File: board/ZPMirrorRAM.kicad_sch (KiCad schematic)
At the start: 15 parts, among them U10 74LS260, U11 74F86, U15 74F00, U21 CY7C192, U22 CY7C192, U23 74F11, U24 74LS154, U25 74F138, U34 74ACT14, U9 74F08

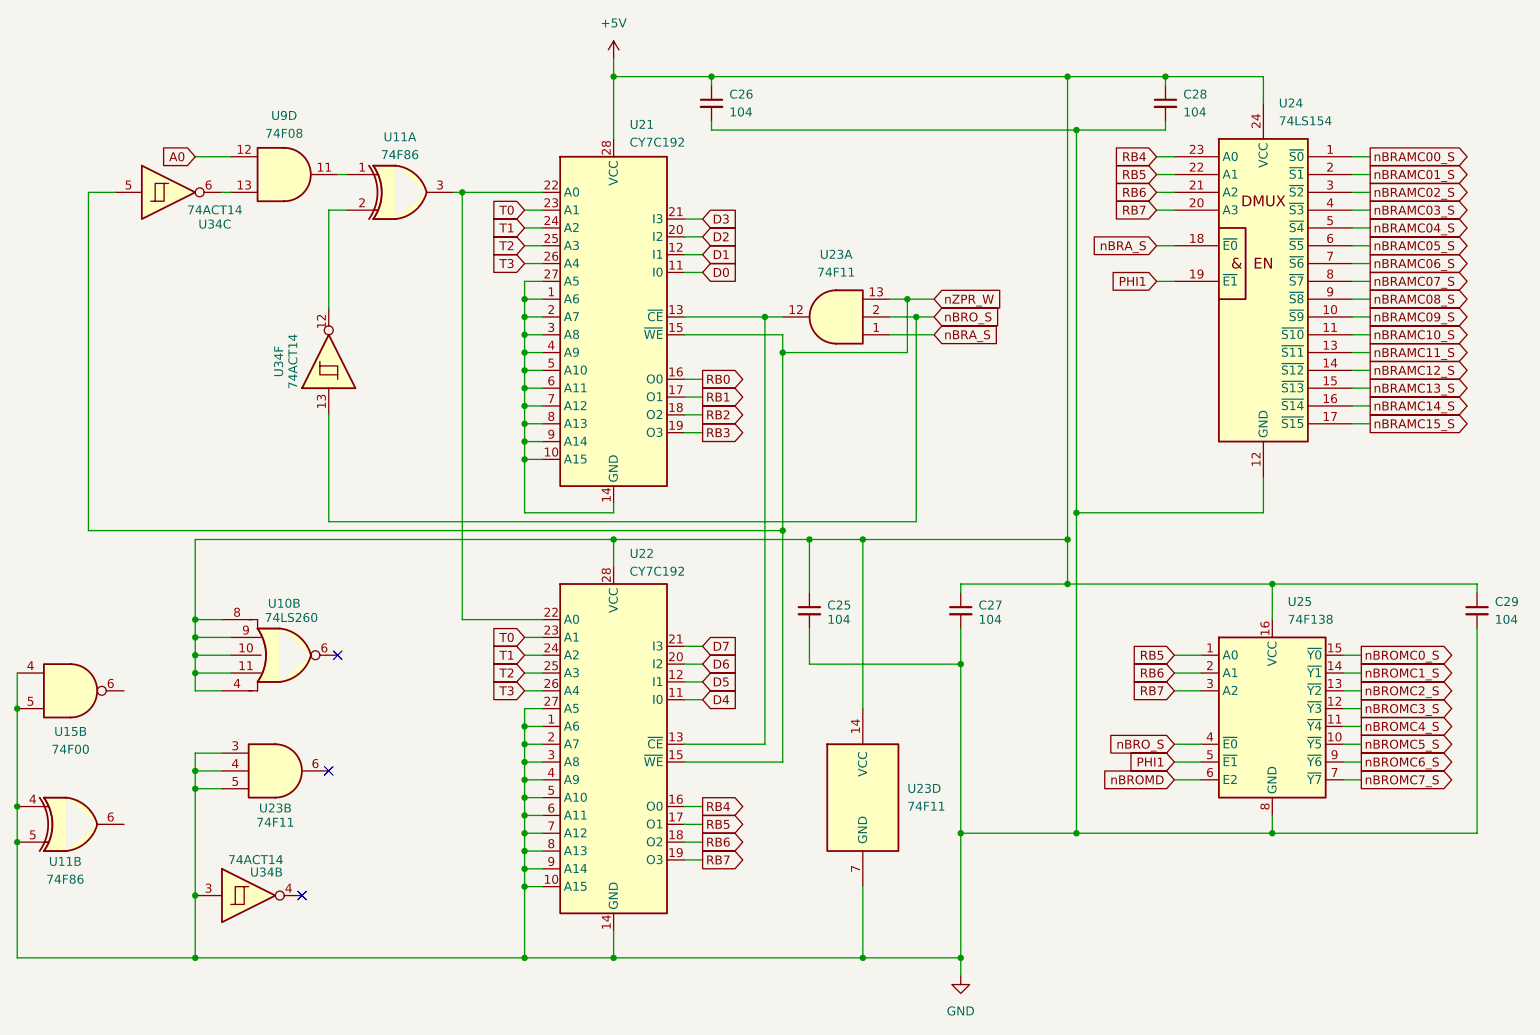
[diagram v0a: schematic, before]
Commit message: V2.0: wait states, GAL glue logic, serial clock and review fixes
Main board schematic:
- Replace the T4-T7 clock divider with RDY wait states. Fixed 7.16 MHz
  CPU clock; J36 selects 3.58 MHz for Rockwell parts. Waits are set per
  region through the write-only register at $FFF5 (reset = 3 waits).
- Move address decode, strobes, the wait-state generator, the IRQ
  encoder/latch/vector mux, ROM bank gating and DMA sync into seven GALs
  (U81-U86 ATF22V10C, U87 ATF16V8C), removing 29 ICs. CUPL sources,
  JEDECs and notes are in board/PLDs/V2.
- 1.8432 MHz serial clock, soft-power latch, -5V regulator, bulk caps,
  pull-ups, audio coupling/decoupling, GNDA tie, read-only Z register
  and other design-review fixes.
- New WaitStates and Support sheets; project symbol library
  hydra16.kicad_sym with sym-lib-table.

PCB updated from the schematic. Includes pending changes to the counter,
bus breakout and memory daughter card projects.

Firmware:
- Remove S_REGISTER; T/U/V/W now at $FFF0-$FFF3 to match the hardware.
- Add math.s and sound.s (included by os_main.s).
- Rebuild the 65C02 ROM image.

Co-Authored-By: Claude Opus 5.5 <noreply@anthropic.com>
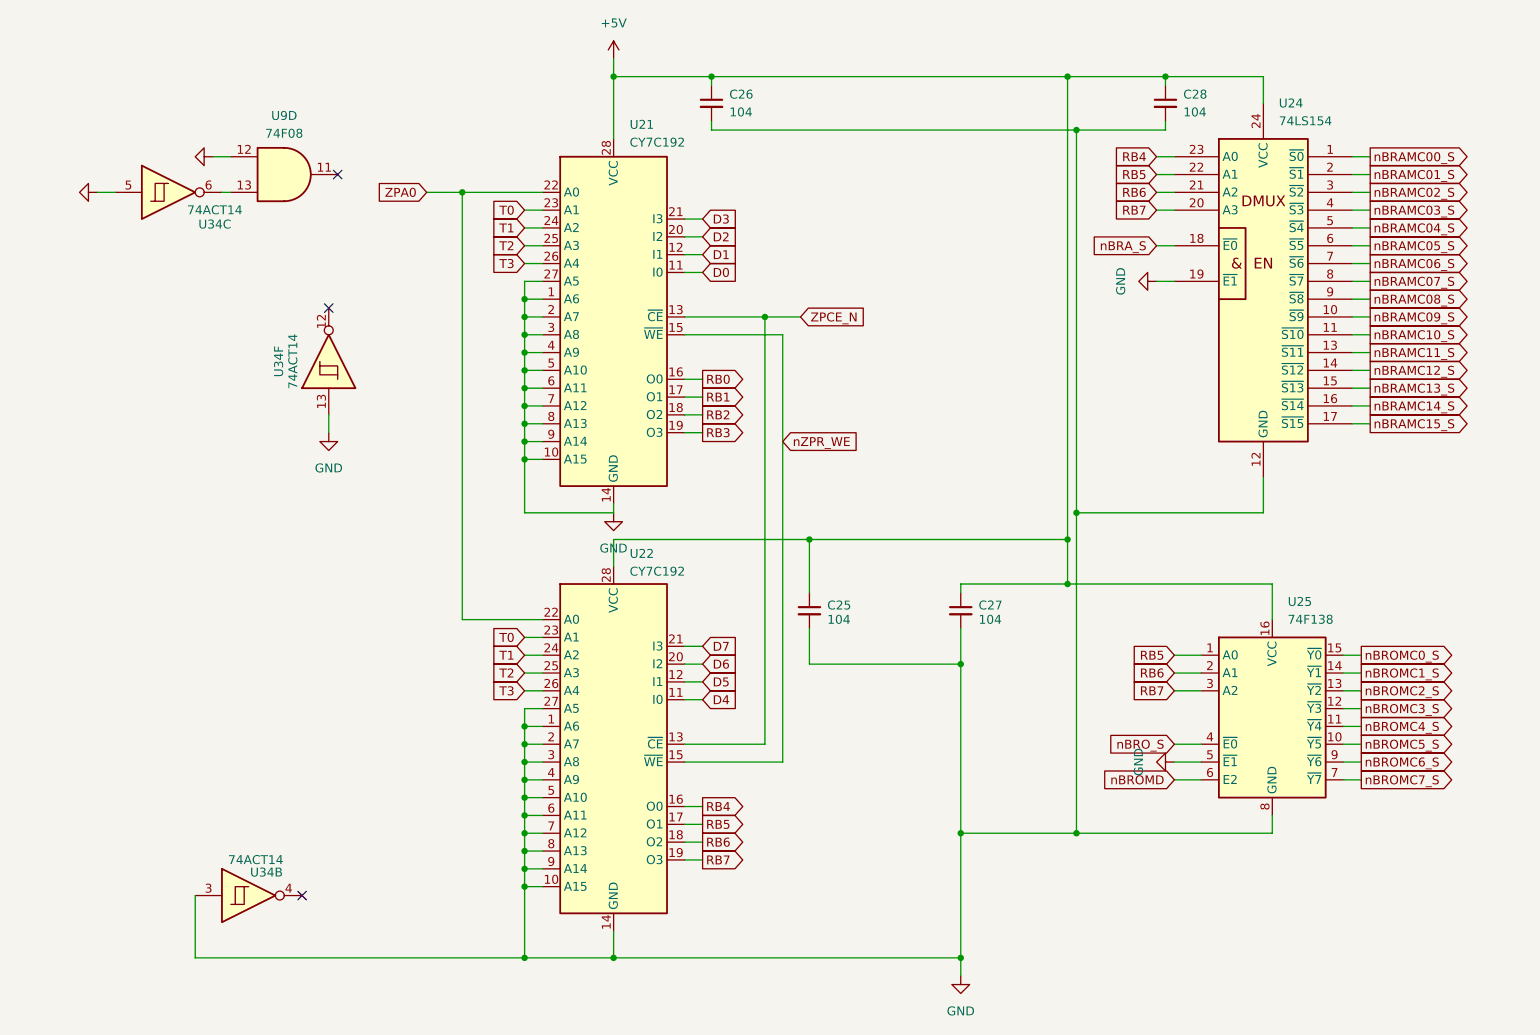
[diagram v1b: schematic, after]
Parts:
- removed C29: 104, Capacitor_THT:C_Disc_D5.0mm_W2.5mm_P5.00mm, symbol Device:C_Small
- removed U10: 74LS260, Package_DIP:DIP-14_W7.62mm_Socket_LongPads, symbol Other_TTL:74LS260
- removed U11: 74F86, Package_DIP:DIP-14_W7.62mm_Socket_LongPads, symbol 74xx:74LS86
- removed U15: 74F00, Package_DIP:DIP-14_W7.62mm_Socket_LongPads, symbol 74xx:74LS00
- removed U23: 74F11, Package_DIP:DIP-14_W7.62mm_Socket_LongPads, symbol 74xx:74LS11
- U21, U22: symbol 65XX:6551 -> Hydra16:CY7C192
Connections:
- net A0 is gone; now on net GND: U9.12
- net PHI1 is gone; now on net GND: U24.19 (~{E1}), U25.5 (~{E1})
- net GND: now also U21.1 (A6), U21.10 (A15), U21.14 (GND), U21.2 (A7), U21.27 (A5), U21.3 (A8), U21.4 (A9), U21.5 (A10), U21.6 (A11), U21.7 (A12), U21.8 (A13), U21.9 (A14), U34.13, U34.5
- net nBRO_S: no longer U34.13
- net ZPCE_N: now reaches U21.13 (~{CE}), U22.13 (~{CE})
- net ZPA0: now reaches U21.22 (A0), U22.22 (A0)
- net nZPR_W renamed nZPR_WE
- net nZPR_WE: no longer U34.5

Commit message: V2.0 rev 2.0D: clock stretching, OS ROM paging and review fixes
Bus timing:
- New GAL C (U88) generates PHI2/PHI1 and the 3.58 MHz sound clock from
  the 14.318 MHz master, replacing the U35 74F191 divider. J36 now selects
  7.16 or 3.58 MHz.
- Banked RAM, banked ROM and slot I/O ($FF20-$FFEF) get one extra PHI2-low
  period plus 0-3 extra PHI2-high periods set in $FFF5 (GAL D). This
  replaces the on-board RDY wait generator; cards can still pull RDY.
- Write strobes are now hold-time safe: PHI1 comes straight from GAL C
  and RWB_M straight from GAL B2.

Review fixes:
- OS ROM chip enable from a single-level decode, output enable from
  GAL B1; -55 part specified. Full 4K OS ROM paging via GAL G.
- Vector RAM writes only during PHI2; $FFF0-$FFFF no longer slowed.
- YM2151 /WR on RWB_M. U62 removed. RB0-RB7 pull-ups (RN5).
- Slot clocks driven through U56 and U34 with 33R series resistors.
- J38 enables in-system flashing of the banked ROMs.
- W65C22S/W65C51N, AS6C4008, DS1813-5 and CY7C192-25 values; R4 1k.
- J7 pin 8 no longer +5V; +5VA renamed +5VSB; serial handshake loop.
- Sheet titles and revisions, slot symbol pin fixes, and project symbol
  and footprint libraries so the project opens on another machine.

Co-Authored-By: Claude Opus 5.5 <noreply@anthropic.com>
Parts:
- added RN5: 103, Resistor_THT:R_Array_SIP9, symbol Device:R_Network08_US
- U21, U22: value CY7C192 -> CY7C192-25
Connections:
- net +5V: now also RN5.1 (common)
- net RB0: now also RN5.2 (R1)
- net RB1: now also RN5.3 (R2)
- net RB2: now also RN5.4 (R3)
- net RB3: now also RN5.5 (R4)
- net RB4: now also RN5.6 (R5)
- net RB5: now also RN5.7 (R6)
- net RB6: now also RN5.8 (R7)
- net RB7: now also RN5.9 (R8)
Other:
- title: ZeroPage $00/$01 Mirror Memory and RAM/ROM Bank Logic -> Zero-Page Bank Register Mirror

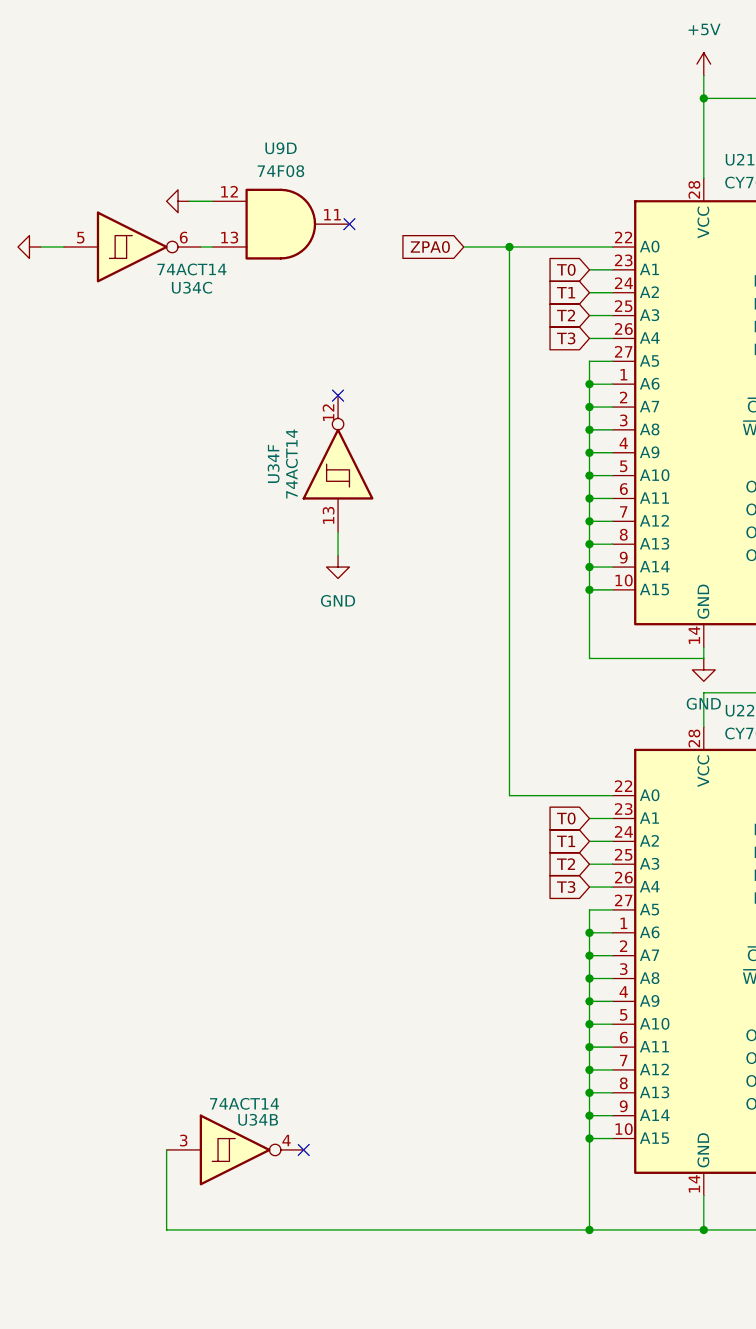
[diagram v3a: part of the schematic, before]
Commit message: V2.0: consolidate parts (239 -> 216), GAL C rev 02
No change in function:
- U9 74F08 removed: GAL C (U88) rev 02 makes the CPU phi0 (P_PHI0 = PHI2
  held low while DMAB_S is low); its decoupling cap C14 removed
- U34 74ACT14 removed: the two clock buffers use spare U19 74F240 gates
- U60 + U61 (2 x CY7C192 vector RAM) replaced by one AS7C256B-15
  (32K x 8, 15 ns); the IRQ sheet's D[0..7] bus is gone
- Crystal oscillators (U75 74HCU04, Y1, Y2, R1, R6-R8, C43, C44, C96,
  C97) replaced by canned oscillators X1 (14.31818 MHz), X2 (1.8432 MHz)
- Soft power: CD40106 -> 74HC14, CD4013 -> 74HC74 (active-low set/reset,
  power-on reset network inverted); a spare 74HC14 gate drives PS_ON#,
  so Q1 is removed
- R10-R13 -> RN6 (4 x 10k, SIP-5); R9, R21-R24 -> RN7 (5 x 33R isolated,
  SIP-10)
- C100-C102 (3 x 220u) -> C100 680u
- Clocks and Power sheet notes updated; PLD README updated

GAL C rev 02 verified against rev 01 over 200,000 clock edges.
PCB updated from the schematic (adds RN6, RN7, X1, X2 and the speakers
LS1/LS2). Also includes KiCad's re-save of the schematic sheets.

Co-Authored-By: Claude Opus 5.5 <noreply@anthropic.com>
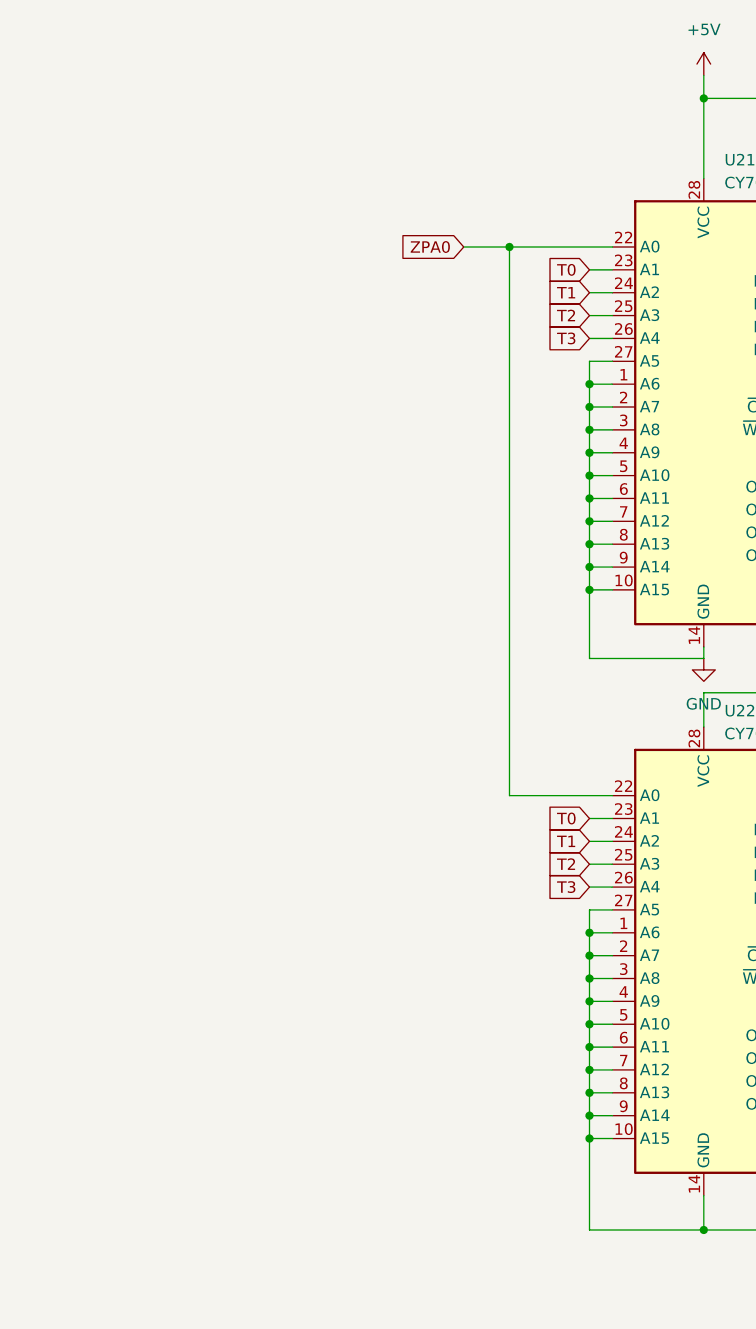
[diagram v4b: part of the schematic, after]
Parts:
- removed U34: 74ACT14, Package_DIP:DIP-14_W7.62mm_Socket_LongPads, symbol 74xx:74HC14
- removed U9: 74F08, Package_DIP:DIP-14_W7.62mm_Socket_LongPads, symbol 74xx:74LS08
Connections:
- no-connect marks 3 -> 0
